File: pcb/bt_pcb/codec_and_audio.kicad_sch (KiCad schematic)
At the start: 17 parts, among them IC2 ADAU1961WBCPZ-R7, J4 Conn_01x01, J5 Conn_01x03

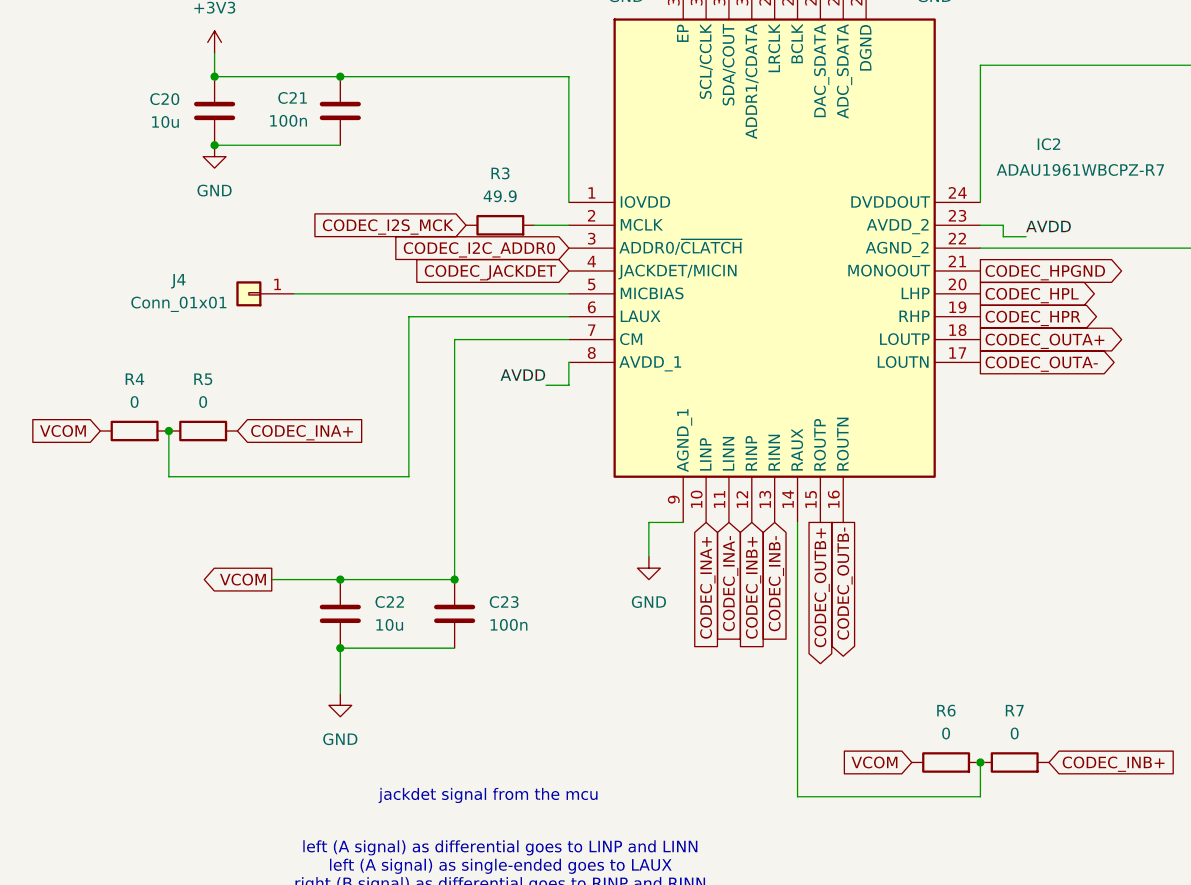
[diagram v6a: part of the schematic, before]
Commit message: pcb with some schematic tuning
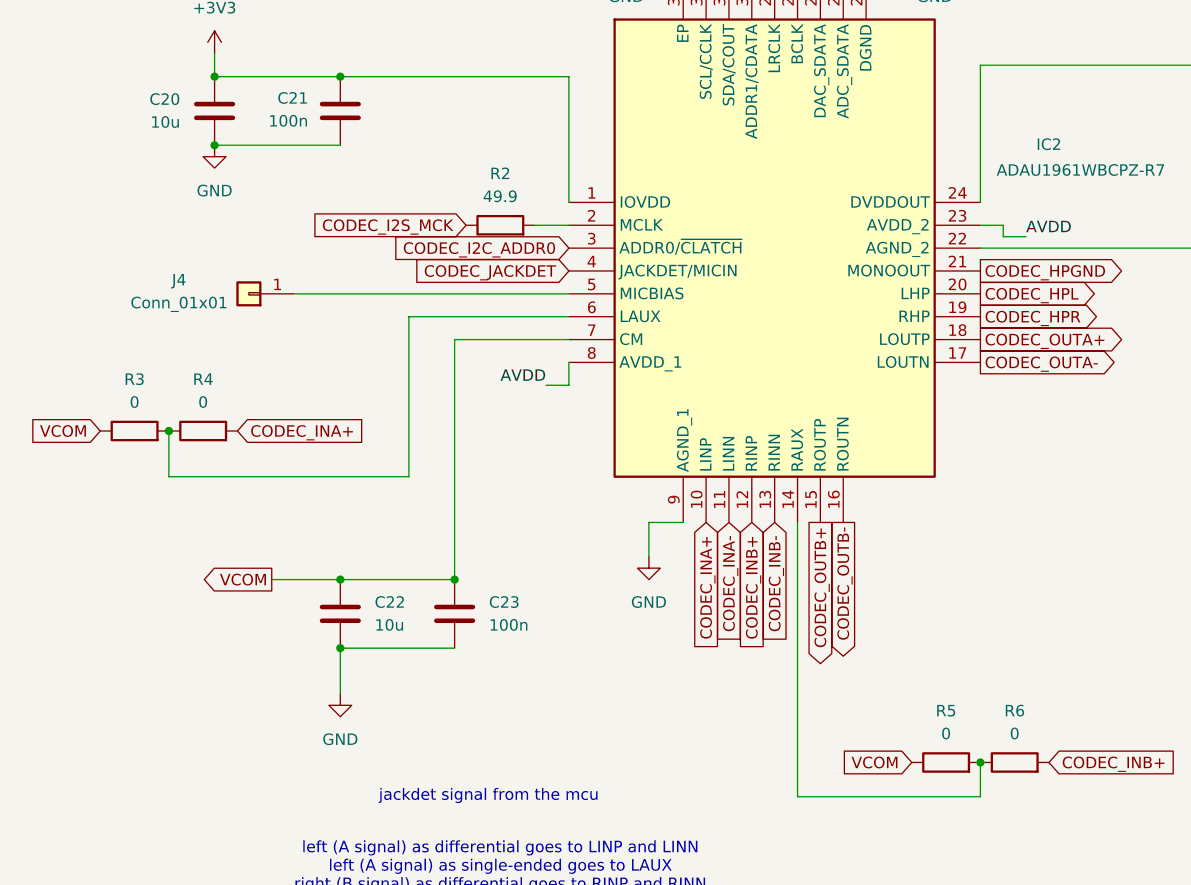
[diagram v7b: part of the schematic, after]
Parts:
- renumbered R3 to R2, R4 to R3, R5 to R4, R6 to R5, R7 to R6
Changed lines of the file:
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@@
 		(dnp no)
 		(fields_autoplaced yes)
-		(property "Reference" "#PWR019"
+		(property "Reference" "#PWR025"
 			(at 62.23 81.28 0)
 			(effects
@@
 			(project ""
 				(path "/eb787481-08cd-41a4-a128-173fa6227c32/4ada0139-8712-47ce-9d4c-ab8fef312f7b"
-					(reference "#PWR019")
+					(reference "#PWR025")
 					(unit 1)
 				)
@@
 		(dnp no)
 		(fields_autoplaced yes)
-		(property "Reference" "#PWR017"
+		(property "Reference" "#PWR023"
 			(at 107.95 72.39 0)
 			(effects
@@
 			(project "bt_pcb"
 				(path "/eb787481-08cd-41a4-a128-173fa6227c32/4ada0139-8712-47ce-9d4c-ab8fef312f7b"
-					(reference "#PWR017")
+					(reference "#PWR023")
 					(unit 1)
 				)
@@
 		(dnp no)
 		(fields_autoplaced yes)
-		(property "Reference" "R4"
+		(property "Reference" "R3"
 			(at 53.34 113.665 90)
 			(effects
@@
 			(project "bt_pcb"
 				(path "/eb787481-08cd-41a4-a128-173fa6227c32/4ada0139-8712-47ce-9d4c-ab8fef312f7b"
-					(reference "R4")
+					(reference "R3")
 					(unit 1)
 				)
@@
 		(dnp no)
 		(fields_autoplaced yes)
-		(property "Reference" "R6"
+		(property "Reference" "R5"
 			(at 143.51 150.495 90)
 			(effects
@@
 			(project "bt_pcb"
 				(path "/eb787481-08cd-41a4-a128-173fa6227c32/4ada0139-8712-47ce-9d4c-ab8fef312f7b"
-					(reference "R6")
+					(reference "R5")
 					(unit 1)
 				)
@@
 		(dnp no)
 		(fields_autoplaced yes)
-		(property "Reference" "#PWR020"
+		(property "Reference" "#PWR026"
 			(at 189.23 92.71 0)
 			(effects
@@
 			(project "bt_pcb"
 				(path "/eb787481-08cd-41a4-a128-173fa6227c32/4ada0139-8712-47ce-9d4c-ab8fef312f7b"
-					(reference "#PWR020")
+					(reference "#PWR026")
 					(unit 1)
 				)
@@
 		(dnp no)
 		(fields_autoplaced yes)
-		(property "Reference" "#PWR023"
+		(property "Reference" "#PWR029"
 			(at 110.49 139.7 0)
 			(effects
@@
 			(project "bt_pcb"
 				(path "/eb787481-08cd-41a4-a128-173fa6227c32/4ada0139-8712-47ce-9d4c-ab8fef312f7b"
-					(reference "#PWR023")
+					(reference "#PWR029")
 					(unit 1)
 				)
@@
 		(dnp no)
 		(fields_autoplaced yes)
-		(property "Reference" "R3"
+		(property "Reference" "R2"
 			(at 93.98 90.805 90)
 			(effects
@@
 			(project ""
 				(path "/eb787481-08cd-41a4-a128-173fa6227c32/4ada0139-8712-47ce-9d4c-ab8fef312f7b"
-					(reference "R3")
+					(reference "R2")
 					(unit 1)
 				)
@@
 		(dnp no)
 		(fields_autoplaced yes)
-		(property "Reference" "#PWR021"
+		(property "Reference" "#PWR027"
 			(at 62.23 93.98 0)
 			(effects
@@
 			(project "bt_pcb"
 				(path "/eb787481-08cd-41a4-a128-173fa6227c32/4ada0139-8712-47ce-9d4c-ab8fef312f7b"
-					(reference "#PWR021")
+					(reference "#PWR027")
 					(unit 1)
 				)
@@
 		(dnp no)
 		(fields_autoplaced yes)
-		(property "Reference" "#PWR015"
+		(property "Reference" "#PWR021"
 			(at 74.93 34.29 0)
 			(effects
@@
 			(project ""
 				(path "/eb787481-08cd-41a4-a128-173fa6227c32/4ada0139-8712-47ce-9d4c-ab8fef312f7b"
-					(reference "#PWR015")
+					(reference "#PWR021")
 					(unit 1)
 				)
@@
 		(dnp no)
 		(fields_autoplaced yes)
-		(property "Reference" "#PWR024"
+		(property "Reference" "#PWR030"
 			(at 76.2 154.94 0)
 			(effects
@@
 			(project "bt_pcb"
 				(path "/eb787481-08cd-41a4-a128-173fa6227c32/4ada0139-8712-47ce-9d4c-ab8fef312f7b"
-					(reference "#PWR024")
+					(reference "#PWR030")
 					(unit 1)
 				)
@@
 		(dnp no)
 		(fields_autoplaced yes)
-		(property "Reference" "R7"
+		(property "Reference" "R6"
 			(at 151.13 150.495 90)
 			(effects
@@
 			(project "bt_pcb"
 				(path "/eb787481-08cd-41a4-a128-173fa6227c32/4ada0139-8712-47ce-9d4c-ab8fef312f7b"
-					(reference "R7")
+					(reference "R6")
 					(unit 1)
 				)
@@
 		(dnp no)
 		(fields_autoplaced yes)
-		(property "Reference" "R5"
+		(property "Reference" "R4"
 			(at 60.96 113.665 90)
 			(effects
@@
 			(project "bt_pcb"
 				(path "/eb787481-08cd-41a4-a128-173fa6227c32/4ada0139-8712-47ce-9d4c-ab8fef312f7b"
-					(reference "R5")
+					(reference "R4")
 					(unit 1)
 				)
@@
 		(dnp no)
 		(fields_autoplaced yes)
-		(property "Reference" "#PWR016"
+		(property "Reference" "#PWR022"
 			(at 74.93 52.07 0)
 			(effects
@@
 			(project "bt_pcb"
 				(path "/eb787481-08cd-41a4-a128-173fa6227c32/4ada0139-8712-47ce-9d4c-ab8fef312f7b"
-					(reference "#PWR016")
+					(reference "#PWR022")
 					(unit 1)
 				)
@@
 		(dnp no)
 		(fields_autoplaced yes)
-		(property "Reference" "#PWR018"
+		(property "Reference" "#PWR024"
 			(at 142.24 72.39 0)
 			(effects
@@
 			(project "bt_pcb"
 				(path "/eb787481-08cd-41a4-a128-173fa6227c32/4ada0139-8712-47ce-9d4c-ab8fef312f7b"
-					(reference "#PWR018")
+					(reference "#PWR024")
 					(unit 1)
 				)
@@
 		(dnp no)
 		(fields_autoplaced yes)
-		(property "Reference" "#PWR022"
+		(property "Reference" "#PWR028"
 			(at 173.99 105.41 0)
 			(effects
@@
 			(project "bt_pcb"
 				(path "/eb787481-08cd-41a4-a128-173fa6227c32/4ada0139-8712-47ce-9d4c-ab8fef312f7b"
-					(reference "#PWR022")
-					(unit 1)
-				)
+					(reference "#PWR028")
+					(unit 1)
+				)

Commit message: pcb now under revision
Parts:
- added C15: 10u, Capacitor_SMD:C_0805_2012Metric_Pad1.18x1.45mm_HandSolder, symbol Device:C
- added C16: 1u, Capacitor_SMD:C_0603_1608Metric_Pad1.08x0.95mm_HandSolder, symbol Device:C
- added C17: 100n, Capacitor_SMD:C_0603_1608Metric_Pad1.08x0.95mm_HandSolder, symbol Device:C
- renumbered C15 to C18, C16 to C19, C17 to C20, C18 to C21, C19 to C22, C20 to C23, C21 to C24, C22 to C25, C23 to C26
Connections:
- net +3.3VA: now also C15.1, C16.1, C17.1
- net GND: now also C15.2, C16.2, C17.2
